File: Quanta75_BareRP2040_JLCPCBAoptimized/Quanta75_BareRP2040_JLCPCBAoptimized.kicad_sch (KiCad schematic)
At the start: 253 parts, among them J1 USB_C_Receptacle_USB2.0, J10 Conn_01x05_Socket GPIOs, J2 Conn_01x02_Socket VBUS 5V, J3 Conn_01x02_Socket 3V3, J5 Conn_01x04_Socket SWD, J6 USB_A_Receptacle_UBS2.0, J7 USB_C_Receptacle_USB2.0, J8 Conn_01x04_Socket I2C display, J9 USB_C_Receptacle_USB2.0, SW1 SW_Push, SW10 SW_Push, SW11 SW_Push, SW12 SW_Push, SW13 SW_Push, SW14 SW_Push, SW15 SW_Push, SW16 SW_Push, SW17 SW_Push, SW18 SW_Push, SW19 SW_Push, SW2 SW_Push, SW20 SW_Push, SW21 SW_Push, SW22 SW_Push, SW23 SW_Push, SW24 SW_Push, SW25 SW_Push, SW26 SW_Push, SW27 SW_Push, SW28 SW_Push, SW29 SW_Push, SW3 SW_Push, SW30 SW_Push, SW31 SW_Push, SW32 SW_Push, SW33 SW_Push, SW34 SW_Push, SW35 SW_Push, SW36 SW_Push, SW37 SW_Push, SW38 SW_Push, SW39 SW_Push, SW4 SW_Push, SW40 SW_Push, SW41 SW_Push, SW42 SW_Push, SW43 SW_Push, SW44 SW_Push, SW45 SW_Push, SW46 SW_Push, SW47 SW_Push, SW48 SW_Push, SW49 SW_Push, SW5 SW_Push, SW50 SW_Push, SW51 SW_Push, SW52 SW_Push, SW53 SW_Push, SW54 SW_Push, SW55 SW_Push, SW56 SW_Push, SW57 SW_Push, SW58 SW_Push, SW59 SW_Push, SW6 SW_Push, SW60 SW_Push, SW61 SW_Push, SW62 SW_Push, SW63 SW_Push, SW64 SW_Push, SW65 SW_Push, SW66 SW_Push, SW67 SW_Push, SW68 SW_Push, SW69 SW_Push, SW7 SW_Push, SW70 SW_Push, SW71 SW_Push, SW72 SW_Push, SW73 SW_Push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

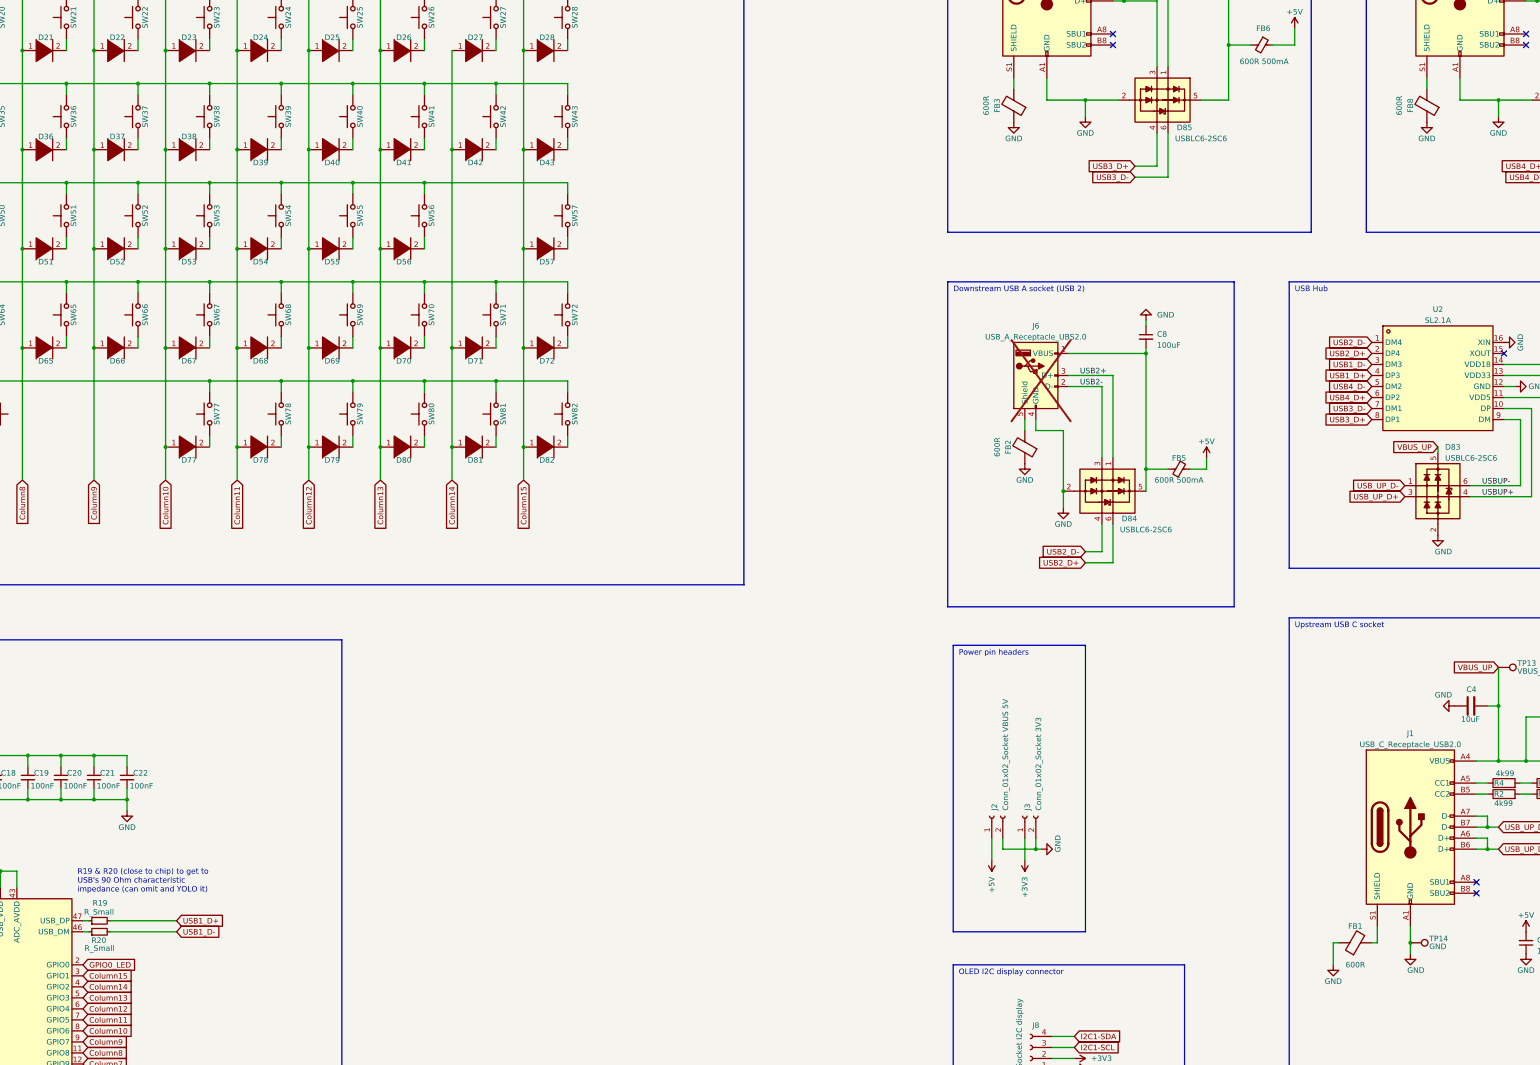
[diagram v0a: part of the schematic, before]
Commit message: additional screw holes
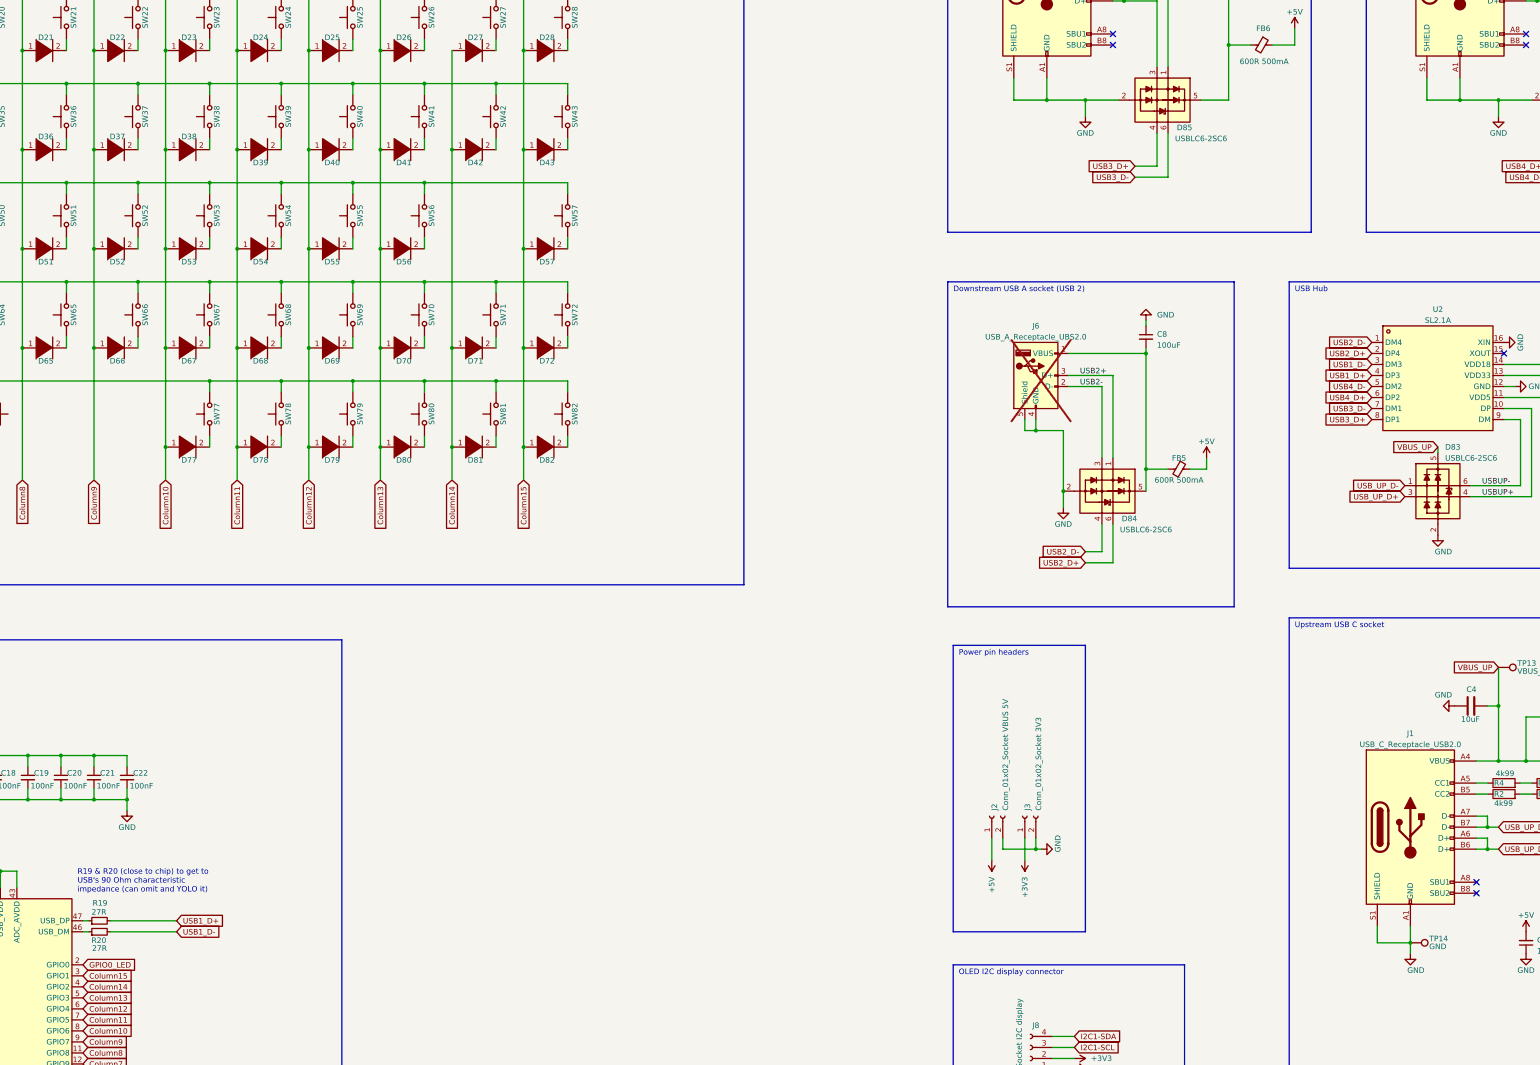
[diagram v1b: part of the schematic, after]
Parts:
- removed FB1, FB2, FB3, FB8: 600R, PCM_Ferrite_SMD_Handsoldering_AKL:Ferrite_0805_2012Metric, symbol Device:FerriteBead
- R19, R20: value R_Small -> 27R
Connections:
- net GND: now also J1.S1 (SHIELD), J6.5 (Shield), J7.S1 (SHIELD), J9.S1 (SHIELD)

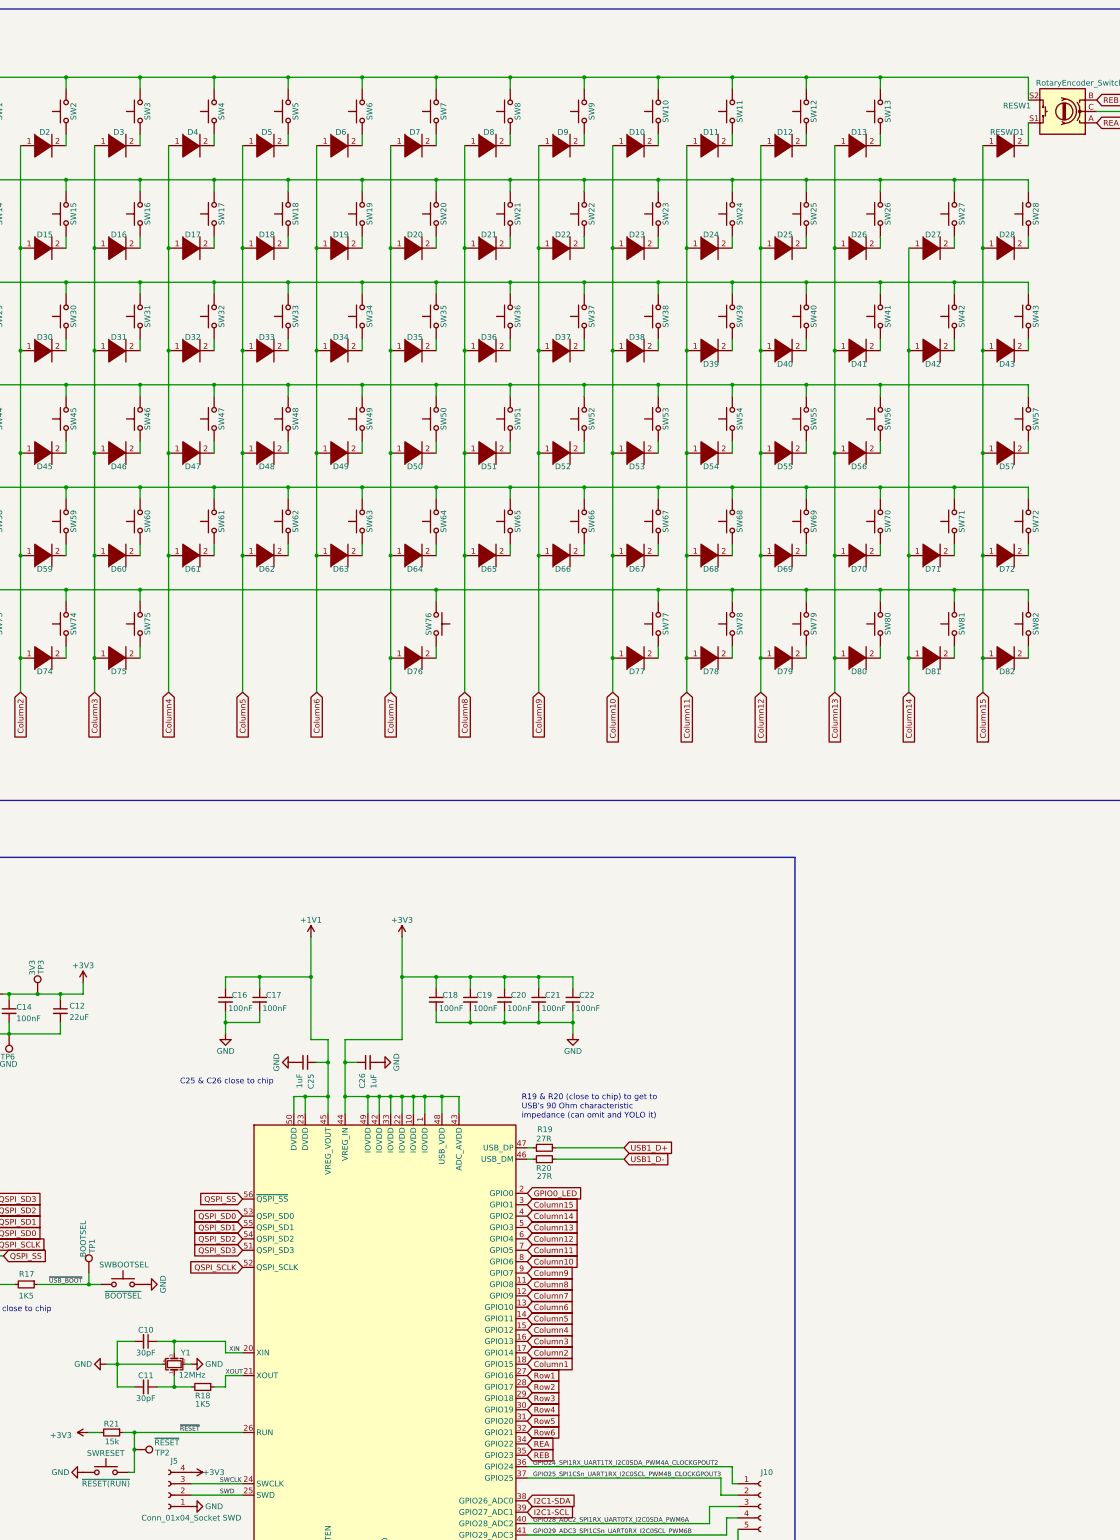
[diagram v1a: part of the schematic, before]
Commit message: link 3D models
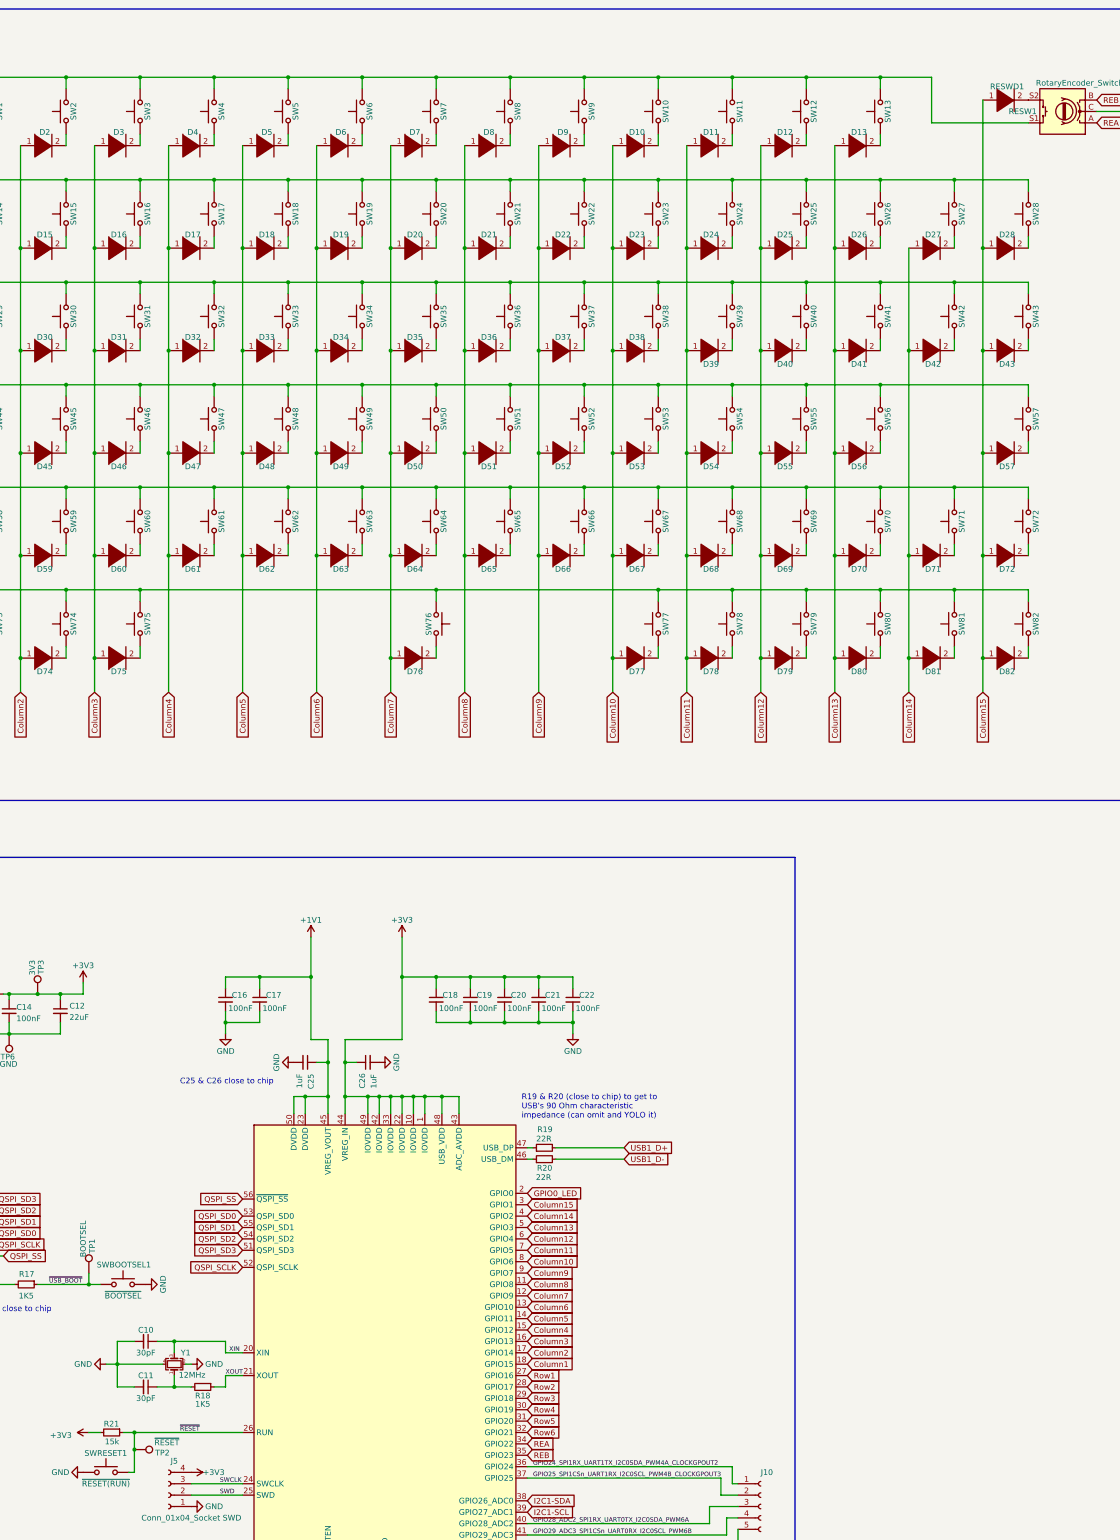
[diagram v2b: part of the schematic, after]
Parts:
- R19, R20: value 27R -> 22R; footprint (none) -> Resistor_SMD:R_0402_1005Metric_Pad0.72x0.64mm_HandSolder; JLCPCB (none) -> C25092
- renumbered SWBOOTSEL to SWBOOTSEL1, SWRESET to SWRESET1
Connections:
- net Row1: now also RESW1.S1; no longer RESW1.S2
- net at RESWD1.2 (A): now also RESW1.S2; no longer RESW1.S1
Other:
- moved on the sheet: RESWD1
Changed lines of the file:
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@@
     (stroke (width 0) (type default))
   )
-  (wire (pts (xy 297.18 40.64) (xy 297.18 45.72))
+  (wire (pts (xy 275.59 40.64) (xy 275.59 50.8))
     (stroke (width 0) (type default))
   )
@@
     (stroke (width 0) (type default))
   )
-  (wire (pts (xy 297.18 50.8) (xy 297.18 55.88))
-    (stroke (width 0) (type default))
-  )
   (wire (pts (xy 422.91 172.72) (xy 422.91 153.67))
     (stroke (width 0) (type default))
@@
     (stroke (width 0) (type default))
   )
-  (wire (pts (xy 264.16 40.64) (xy 297.18 40.64))
+  (wire (pts (xy 264.16 40.64) (xy 275.59 40.64))
     (stroke (width 0) (type default))
   )
@@
     (stroke (width 0) (type default))
   )
-  (wire (pts (xy 287.02 55.88) (xy 287.02 78.74))
+  (wire (pts (xy 287.02 45.72) (xy 287.02 78.74))
     (stroke (width 0) (type default))
   )
@@
     (stroke (width 0) (type default))
   )
+  (wire (pts (xy 275.59 50.8) (xy 297.18 50.8))
+    (stroke (width 0) (type default))
+  )
   (wire (pts (xy 109.22 327.66) (xy 110.49 327.66))
     (stroke (width 0) (type default))
@@
   (symbol (lib_id "Switch:SW_Push") (at 95.25 309.88 0) (unit 1)
     (in_bom yes) (on_board yes) (dnp no)
-    (property "Reference" "SWBOOTSEL" (at 95.4399 305.4889 0)
+    (property "Reference" "SWBOOTSEL1" (at 95.4399 305.4889 0)
       (effects (font (size 1.27 1.27)))
     )
@@
       (project "Quanta75_BareRP2040_JLCPCBAoptimized"
         (path "/0cabb2e6-4a46-4ffe-8ff7-d51fc1f6dda5"
-          (reference "SWBOOTSEL") (unit 1)
+          (reference "SWBOOTSEL1") (unit 1)
         )
       )
@@
   (symbol (lib_id "Device:RotaryEncoder_Switch") (at 304.8 48.26 180) (unit 1)
     (in_bom no) (on_board yes) (dnp no)
-    (property "Reference" "RESW1" (at 294.64 46.99 0)
+    (property "Reference" "RESW1" (at 295.91 48.26 0)
       (effects (font (size 1.27 1.27)))
     )
@@
     )
   )
+  (symbol (lib_id "Device:R_Small") (at 189.23 281.94 90) (unit 1)
+    (in_bom yes) (on_board yes) (dnp no)
+    (property "Reference" "R20" (at 189.281 283.9145 90)
+      (effects (font (size 1.27 1.27)))
+    )
+    (property "Value" "22R" (at 189.0438 285.997 90)
+      (effects (font (size 1.27 1.27)))
+    )
+    (property "Footprint" "Resistor_SMD:R_0402_1005Metric_Pad0.72x0.64mm_HandSolder" (at 189.23 281.94 0)
+      (effects (font (size 1.27 1.27)) hide)
+    )
+    (property "Datasheet" "~" (at 189.23 281.94 0)
+      (effects (font (size 1.27 1.27)) hide)
+    )
+    (property "JLCPCB" "C25092" (at 189.23 281.94 90)
+      (effects (font (size 1.27 1.27)) hide)
+    )
+    (pin "1")
+    (pin "2")
+    (instances
+      (project "Quanta75_BareRP2040_JLCPCBAoptimized"
+        (path "/0cabb2e6-4a46-4ffe-8ff7-d51fc1f6dda5"
+          (reference "R20") (unit 1)
+        )
+      )
+    )
+  )
   (symbol (lib_id "pspice:DIODE") (at 226.06 55.88 0) (unit 1)
     (in_bom yes) (on_board yes) (dnp no)
@@
     )
   )
-  (symbol (lib_id "Device:R_Small") (at 189.23 281.94 90) (unit 1)
-    (in_bom yes) (on_board yes) (dnp no)
-    (property "Reference" "R20" (at 189.0919 283.931 90)
-      (effects (font (size 1.27 1.27)))
-    )
-    (property "Value" "27R" (at 189.23 285.75 90)
-      (effects (font (size 1.27 1.27)))
-    )
-    (property "Footprint" "" (at 189.23 281.94 0)
-      (effects (font (size 1.27 1.27)) hide)
-    )
-    (property "Datasheet" "~" (at 189.23 281.94 0)
-      (effects (font (size 1.27 1.27)) hide)
-    )
-    (pin "1")
-    (pin "2")
-    (instances
-      (project "Quanta75_BareRP2040_JLCPCBAoptimized"
-        (path "/0cabb2e6-4a46-4ffe-8ff7-d51fc1f6dda5"
-          (reference "R20") (unit 1)
-        )
-      )
-    )
-  )
   (symbol (lib_name "SW_Push_1") (lib_id "Switch:SW_Push") (at 99.06 48.26 90) (unit 1)
     (in_bom yes) (on_board yes) (dnp no)
@@
     )
   )
-  (symbol (lib_id "pspice:DIODE") (at 292.1 55.88 0) (unit 1)
+  (symbol (lib_id "pspice:DIODE") (at 292.1 45.72 0) (unit 1)
     (in_bom yes) (on_board yes) (dnp no)
-    (property "Reference" "RESWD1" (at 292.4253 52.8798 0)
+    (property "Reference" "RESWD1" (at 292.4253 42.7198 0)
       (effects (font (size 1.27 1.27)))
     )
-    (property "Value" "DIODE" (at 292.1 59.69 0)
+    (property "Value" "DIODE" (at 292.1 49.53 0)
       (effects (font (size 1.27 1.27)) hide)
     )
-    (property "Footprint" "Diode_SMD:D_SOD-123" (at 292.1 55.88 0)
+    (property "Footprint" "Diode_SMD:D_SOD-123" (at 292.1 45.72 0)
       (effects (font (size 1.27 1.27)) hide)
     )
-    (property "Datasheet" "~" (at 292.1 55.88 0)
+    (property "Datasheet" "~" (at 292.1 45.72 0)
       (effects (font (size 1.27 1.27)) hide)
     )
@@
   (symbol (lib_id "Switch:SW_Push") (at 91.44 351.79 0) (unit 1)
     (in_bom yes) (on_board yes) (dnp no)
-    (property "Reference" "SWRESET" (at 91.3964 347.5239 0)
+    (property "Reference" "SWRESET1" (at 91.3964 347.5239 0)
       (effects (font (size 1.27 1.27)))
     )
@@
       (project "Quanta75_BareRP2040_JLCPCBAoptimized"
         (path "/0cabb2e6-4a46-4ffe-8ff7-d51fc1f6dda5"
-          (reference "SWRESET") (unit 1)
+          (reference "SWRESET1") (unit 1)
         )
       )
@@
       (effects (font (size 1.27 1.27)))
     )
-    (property "Value" "27R" (at 189.1136 277.3918 90)
+    (property "Value" "22R" (at 189.1136 277.3918 90)
       (effects (font (size 1.27 1.27)))
     )
-    (property "Footprint" "" (at 189.23 279.4 0)
+    (property "Footprint" "Resistor_SMD:R_0402_1005Metric_Pad0.72x0.64mm_HandSolder" (at 189.23 279.4 0)
       (effects (font (size 1.27 1.27)) hide)
     )
@@
       (effects (font (size 1.27 1.27)) hide)
     )
+    (property "JLCPCB" "C25092" (at 189.23 279.4 90)
+      (effects (font (size 1.27 1.27)) hide)
+    )

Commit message: add oshw logo
OSHW BE10
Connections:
- net RP2040_D-: now reaches R20.1, U1.46 (USB_DM)
- net RP2040_D+: now reaches R19.1, U1.47 (USB_DP)
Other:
- note added: "C25 close to VREG_VOUT"
- note added: "C26 close to VREG_IN"
- note removed: "C25 & C26 close to chip"
- title: Quanta Keyboard Schematic Bare (RP2040 JLCPCBA) -> Quanta75 Keyboard Schematic Bare (RP2040 JLCPCBA)
- moved on the sheet: C16, C17, C25, C26, R19, R20
